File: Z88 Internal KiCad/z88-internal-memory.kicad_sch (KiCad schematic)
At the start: 8 parts, among them J1 Conn_01x02, U1 M29F400, U2 IS61C5128AS-25TLI

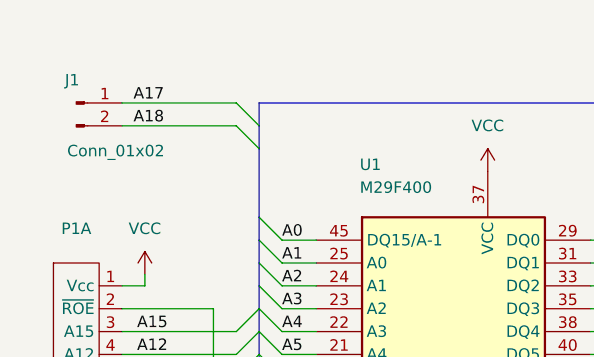
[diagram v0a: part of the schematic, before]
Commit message: updated silkscreen
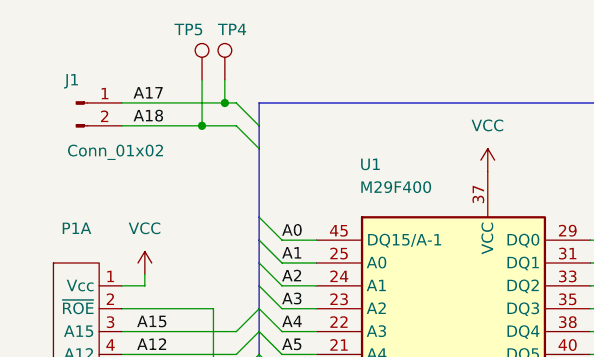
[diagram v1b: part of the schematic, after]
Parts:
- added TP4, TP5: TestPoint, Z88 internal memory:TestPoint, symbol Connector:TestPoint
- TP1: footprint TestPoint:TestPoint_THTPad_D1.5mm_Drill0.7mm -> Z88 internal memory:TestPoint
- TP2: value RAM 3 -> A14; footprint TestPoint:TestPoint_THTPad_D1.5mm_Drill0.7mm -> Z88 internal memory:TestPoint
- TP3: value RAM 2 -> A16; footprint TestPoint:TestPoint_THTPad_D1.5mm_Drill0.7mm -> Z88 internal memory:TestPoint
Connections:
- net A17: now also TP4.1
- net A18: now also TP5.1
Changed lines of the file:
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@@
 	)
 	(junction
+		(at 73.66 55.88)
+		(diameter 0)
+		(color 0 0 0 0)
+	)
+	(junction
+		(at 71.12 58.42)
+		(diameter 0)
+		(color 0 0 0 0)
+	)
+	(junction
 		(at 124.46 152.4)
 		(diameter 0)
@@
 	(wire
 		(pts
-			(xy 62.23 55.88) (xy 74.93 55.88)
+			(xy 62.23 55.88) (xy 73.66 55.88)
 		)
 		(stroke
@@
 	(wire
 		(pts
+			(xy 73.66 55.88) (xy 74.93 55.88)
+		)
+		(stroke
+			(width 0)
+			(type default)
+		)
+	)
+	(wire
+		(pts
 			(xy 74.93 147.32) (xy 74.93 127)
 		)
@@
 	(wire
 		(pts
+			(xy 73.66 53.34) (xy 73.66 55.88)
+		)
+		(stroke
+			(width 0)
+			(type default)
+		)
+	)
+	(wire
+		(pts
 			(xy 72.39 78.74) (xy 72.39 124.46)
 		)
@@
 	(wire
 		(pts
-			(xy 62.23 58.42) (xy 74.93 58.42)
+			(xy 62.23 58.42) (xy 71.12 58.42)
 		)
 		(stroke
@@
 		)
 	)
+	(wire
+		(pts
+			(xy 71.12 58.42) (xy 74.93 58.42)
+		)
+		(stroke
+			(width 0)
+			(type default)
+		)
+	)
 	(bus
 		(pts
@@
 		)
 	)
+	(wire
+		(pts
+			(xy 71.12 53.34) (xy 71.12 58.42)
+		)
+		(stroke
+			(width 0)
+			(type default)
+		)
+	)
 	(bus
 		(pts
@@
 			)
 		)
-		(property "Footprint" "TestPoint:TestPoint_THTPad_D1.5mm_Drill0.7mm"
+		(property "Footprint" "Z88 internal memory:TestPoint"
 			(at 125.73 118.11 0)
 			(effects
@@
 			)
 		)
-		(property "Value" "RAM 2"
+		(property "Value" "A16"
 			(at 136.398 81.28 90)
 			(effects
@@
 			)
 		)
-		(property "Footprint" "TestPoint:TestPoint_THTPad_D1.5mm_Drill0.7mm"
+		(property "Footprint" "Z88 internal memory:TestPoint"
 			(at 139.7 78.74 0)
 			(effects
@@
 	)
 	(symbol
+		(lib_id "Connector:TestPoint")
+		(at 73.66 53.34 0)
+		(unit 1)
+		(exclude_from_sim no)
+		(in_bom yes)
+		(on_board yes)
+		(dnp no)
+		(property "Reference" "TP4"
+			(at 72.898 47.752 0)
+			(effects
+				(font
+					(size 1.27 1.27)
+				)
+				(justify left)
+			)
+		)
+		(property "Value" "TestPoint"
+			(at 76.2 51.3079 0)
+			(effects
+				(font
+					(size 1.27 1.27)
+				)
+				(justify left)
+				(hide yes)
+			)
+		)
+		(property "Footprint" "Z88 internal memory:TestPoint"
+			(at 78.74 53.34 0)
+			(effects
+				(font
+					(size 1.27 1.27)
+				)
+				(hide yes)
+			)
+		)
+		(property "Datasheet" "~"
+			(at 78.74 53.34 0)
+			(effects
+				(font
+					(size 1.27 1.27)
+				)
+				(hide yes)
+			)
+		)
+		(property "Description" "test point"
+			(at 73.66 53.34 0)
+			(effects
+				(font
+					(size 1.27 1.27)
+				)
+				(hide yes)
+			)
+		)
+		(pin "1"
+		)
+		(instances
+			(project ""
+				(path "/823d07c1-a4bc-4412-a610-b2ea7bb3dc09"
+					(reference "TP4")
+					(unit 1)
+				)
+			)
+		)
+	)
+	(symbol
 		(lib_id "power:GND")
 		(at 64.77 118.11 0)
@@
 	)
 	(symbol
+		(lib_id "Connector:TestPoint")
+		(at 71.12 53.34 0)
+		(unit 1)
+		(exclude_from_sim no)
+		(in_bom yes)
+		(on_board yes)
+		(dnp no)
+		(property "Reference" "TP5"
+			(at 68.072 47.752 0)
+			(effects
+				(font
+					(size 1.27 1.27)
+				)
+				(justify left)
+			)
+		)
+		(property "Value" "TestPoint"
+			(at 73.66 51.3079 0)
+			(effects
+				(font
+					(size 1.27 1.27)
+				)
+				(justify left)
+				(hide yes)
+			)
+		)
+		(property "Footprint" "Z88 internal memory:TestPoint"
+			(at 76.2 53.34 0)
+			(effects
+				(font
+					(size 1.27 1.27)
+				)
+				(hide yes)
+			)
+		)
+		(property "Datasheet" "~"
+			(at 76.2 53.34 0)
+			(effects
+				(font
+					(size 1.27 1.27)
+				)
+				(hide yes)
+			)
+		)
+		(property "Description" "test point"
+			(at 71.12 53.34 0)
+			(effects
+				(font
+					(size 1.27 1.27)
+				)
+				(hide yes)
+			)
+		)
+		(pin "1"
+		)
+		(instances
+			(project ""
+				(path "/823d07c1-a4bc-4412-a610-b2ea7bb3dc09"
+					(reference "TP5")
+					(unit 1)
+				)
+			)
+		)
+	)
+	(symbol
 		(lib_id "Z88 RAM ROM Internal:ROM Pins DIP32")
 		(at 57.15 72.39 0)
@@
 			)
 		)
-		(property "Value" "RAM 3"
+		(property "Value" "A14"
 			(at 136.398 86.36 90)
 			(effects
@@
 			)
 		)
-		(property "Footprint" "TestPoint:TestPoint_THTPad_D1.5mm_Drill0.7mm"
+		(property "Footprint" "Z88 internal memory:TestPoint"
 			(at 139.7 83.82 0)
 			(effects

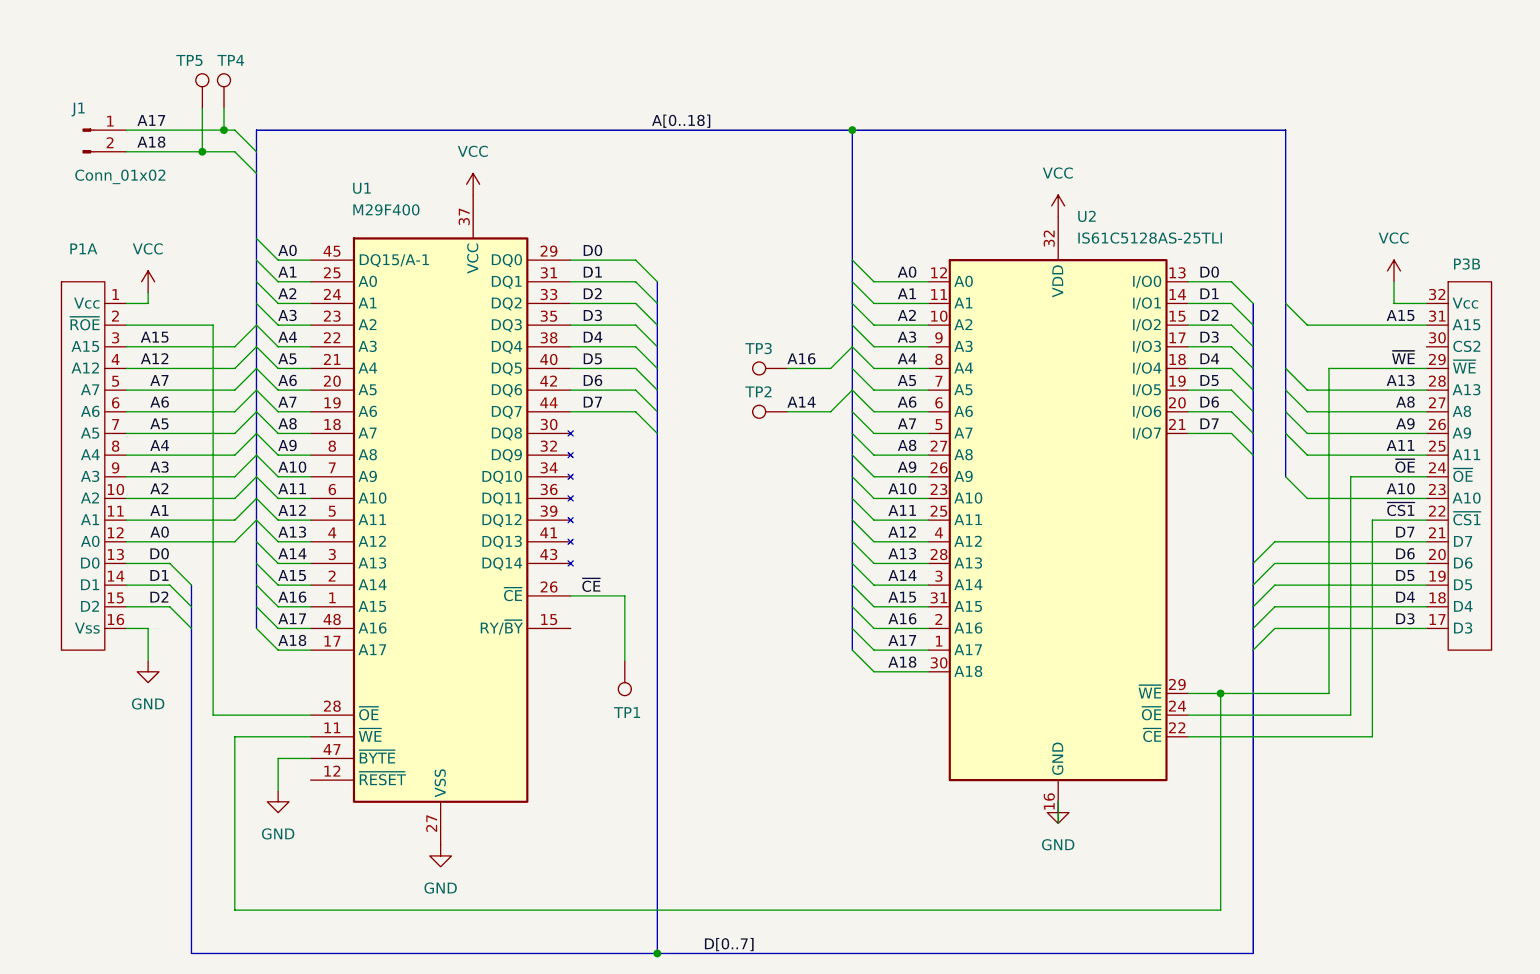
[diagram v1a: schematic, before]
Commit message: layout tweaks, added correct machined-pin headers
3D model and new footprint for pin headers, with silkscreening for back of board mounting
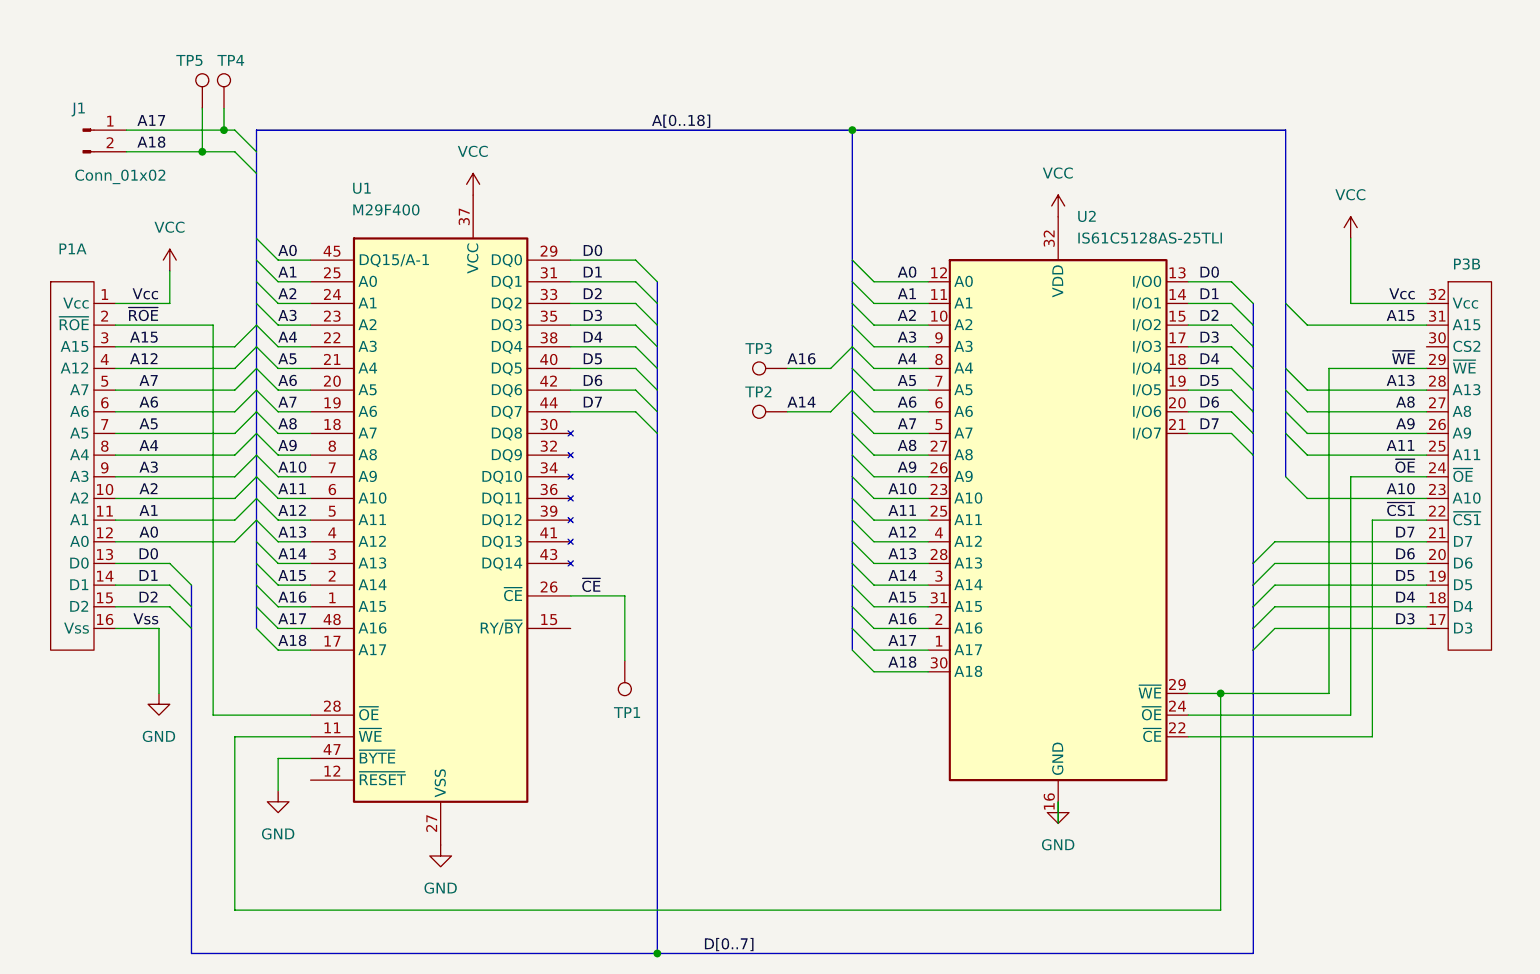
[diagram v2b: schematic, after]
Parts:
- P1: footprint Package_DIP_Custom:DIP-32_W_Left -> Connector_SIP_Header:SIPHeader_1x16_Vertical_P1
- P3: footprint Package_DIP_Custom:DIP-32_W_Right -> Connector_SIP_Header:SIPHeader_1x16_Vertical
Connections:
- net ~{ROE}: now reaches P1.2 (~{ROE}), U1.28 (~{OE})
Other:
- moved on the sheet: P1A

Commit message: added bypass caps, pre-production tweaks
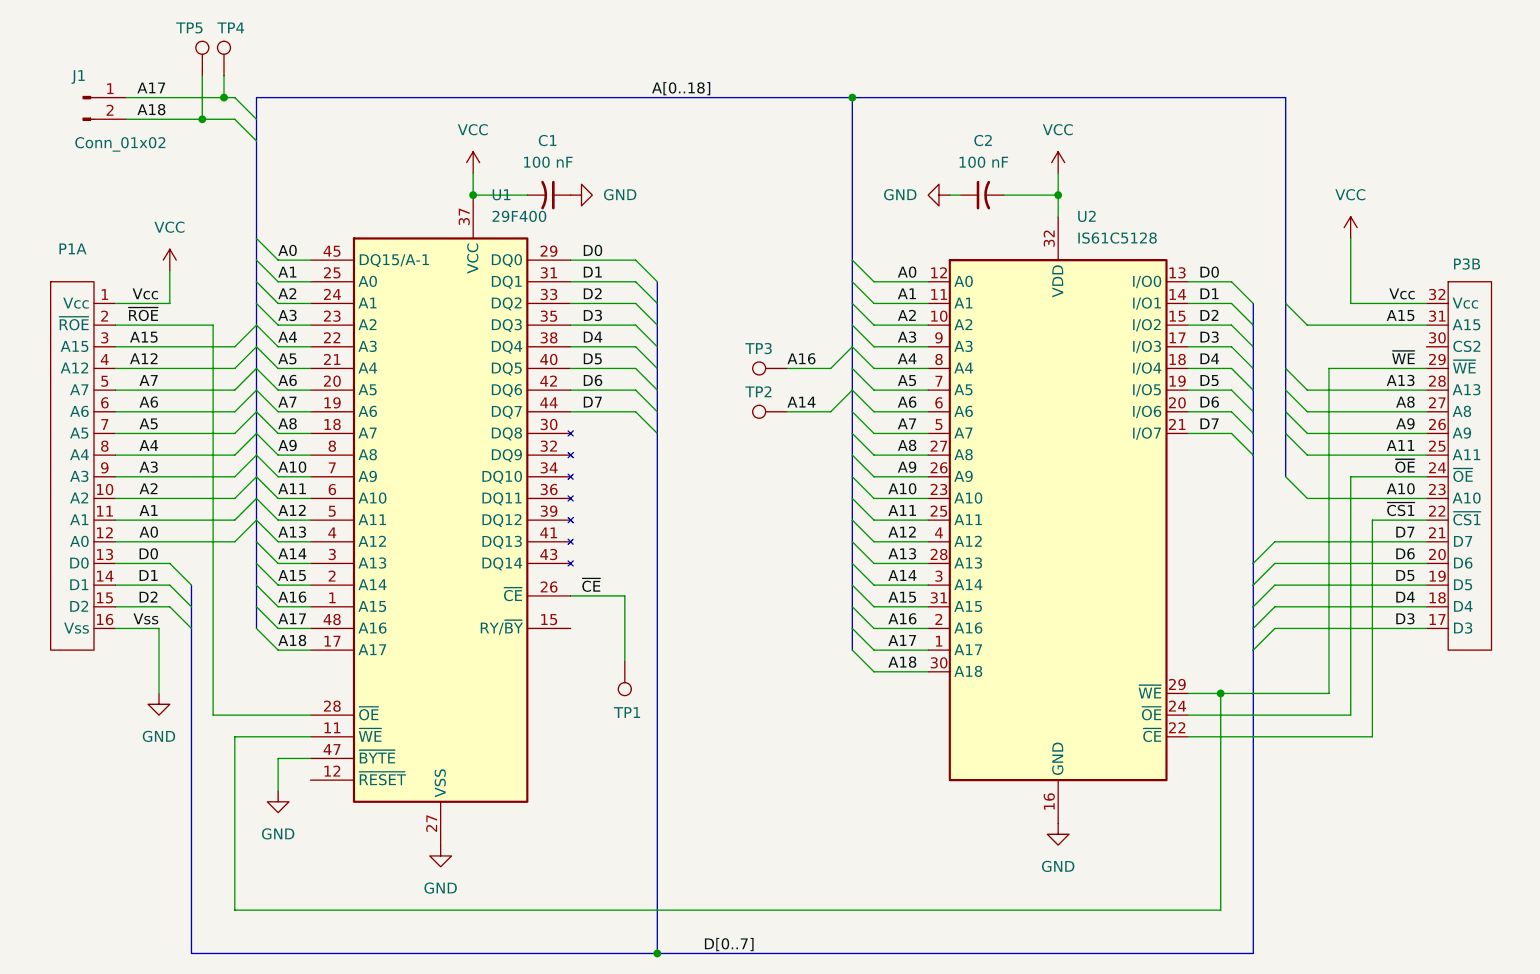
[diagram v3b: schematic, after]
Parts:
- added C1, C2: 100 nF, Capacitor_SMD:C_2220_5750Metric_Pad1.97x5.40mm_HandSolder, symbol Device:C_Small_US
- U1: value M29F400 -> 29F400
- U2: value IS61C5128AS-25TLI -> IS61C5128
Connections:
- net GND: now also C1.1, C2.1
- net VCC: now also C1.2, C2.2
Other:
- moved on the sheet: J1, TP4, TP5
